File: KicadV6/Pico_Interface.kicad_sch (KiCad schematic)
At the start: 3 parts, among them J1 Conn_02x05_Odd_Even, J2 Conn_01x03_Male, U1 Pico

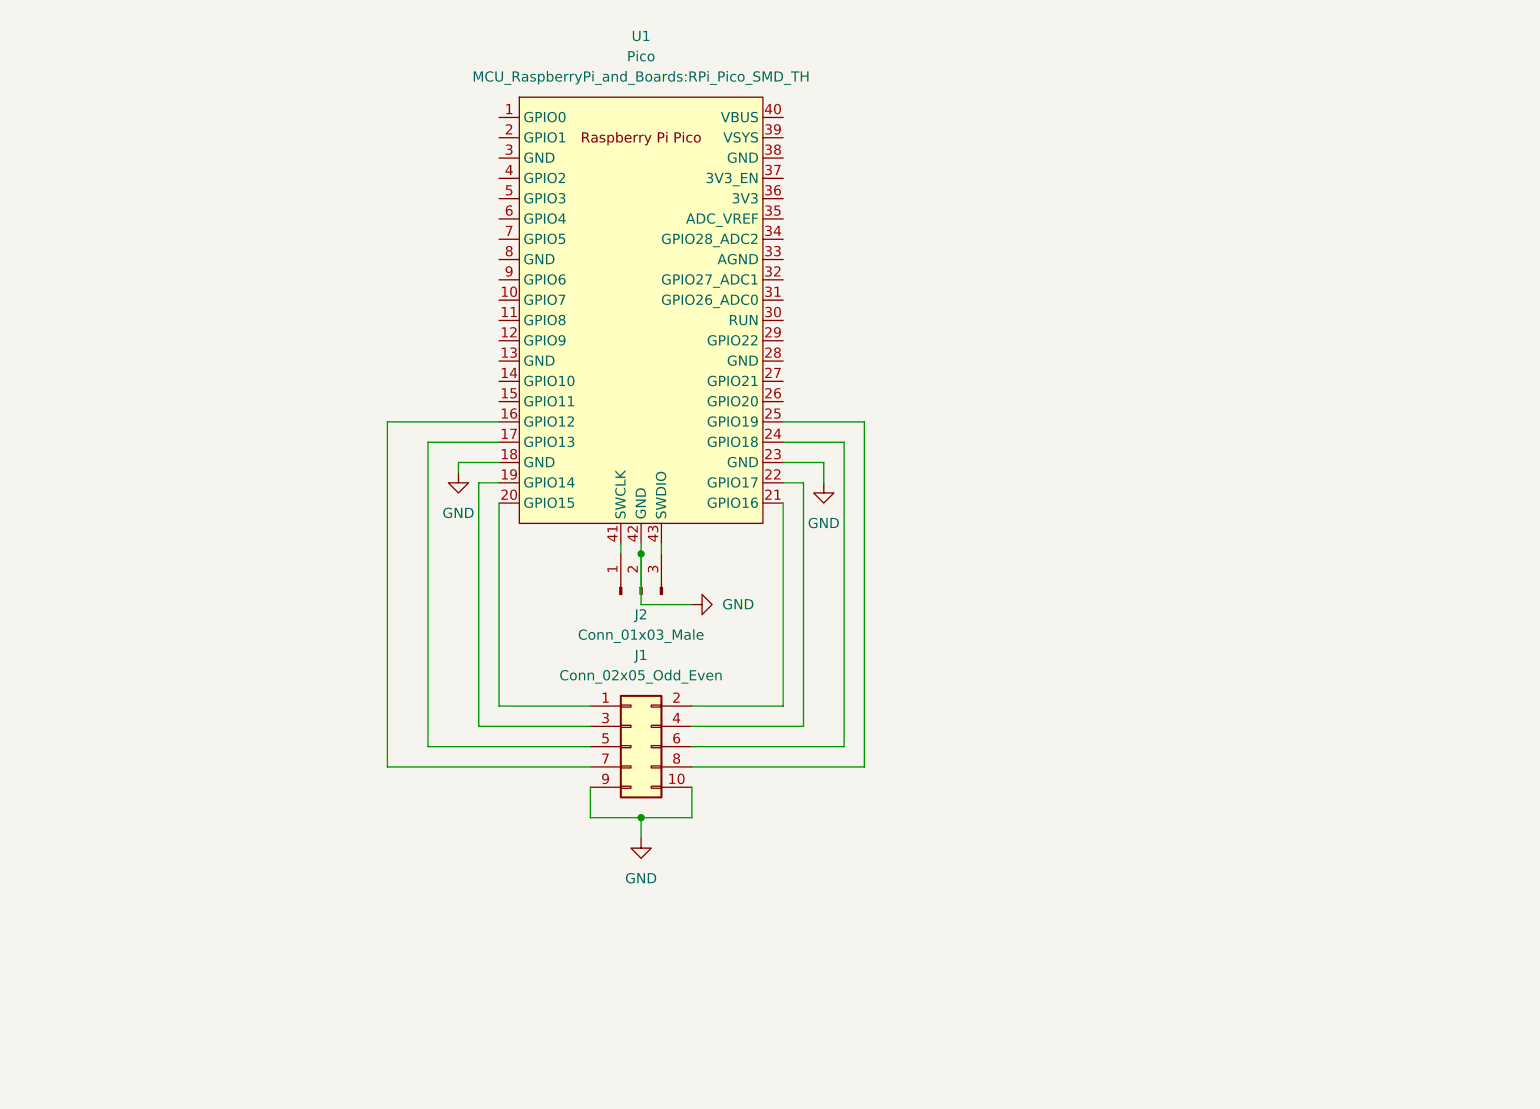
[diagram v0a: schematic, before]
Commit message: Added 4 PMOD / IDC Connectors
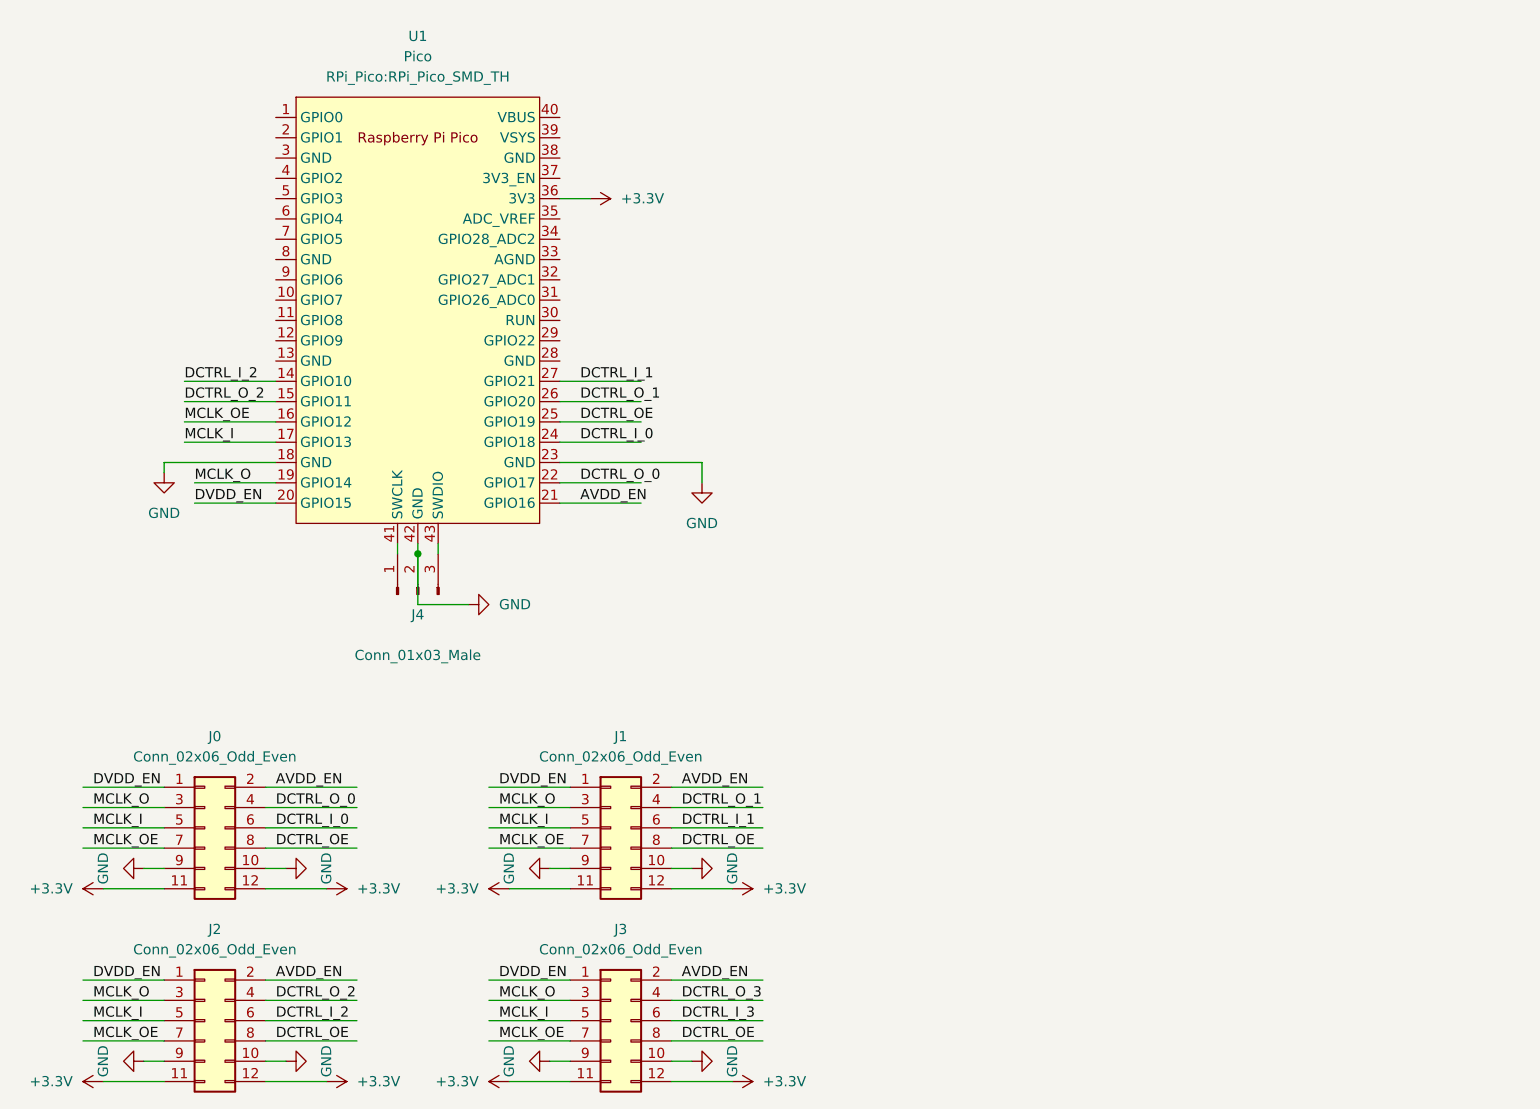
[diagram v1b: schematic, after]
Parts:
- removed J1: Conn_02x05_Odd_Even, Connector_IDC:IDC-Header_2x05_P2.54mm_Horizontal, symbol Connector_Generic:Conn_02x05_Odd_Even
- added J0, J1, J2, J3: Conn_02x06_Odd_Even, Connector_IDC:IDC-Header_2x06_P2.54mm_Vertical, symbol Connector_Generic:Conn_02x06_Odd_Even
- U1: footprint MCU_RaspberryPi_and_Boards:RPi_Pico_SMD_TH -> RPi_Pico:RPi_Pico_SMD_TH
- renumbered J2 to J4
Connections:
- net GND: now also J0.10 (Pin_10), J0.9 (Pin_9), J1.10 (Pin_10), J1.9 (Pin_9), J2.10 (Pin_10), J2.9 (Pin_9), J3.10 (Pin_10), J3.9 (Pin_9)
- net DVDD_EN: now reaches U1.20 (GPIO15)
- net DVDD_EN: now also J0.1 (Pin_1), J1.1 (Pin_1), J2.1 (Pin_1), J3.1 (Pin_1)
- net AVDD_EN: now reaches U1.21 (GPIO16)
- net AVDD_EN: now also J0.2 (Pin_2), J1.2 (Pin_2), J2.2 (Pin_2), J3.2 (Pin_2)
- net MCLK_O: now reaches U1.19 (GPIO14)
- net MCLK_O: now also J0.3 (Pin_3), J1.3 (Pin_3), J2.3 (Pin_3), J3.3 (Pin_3)
- net DCTRL_O_0: now reaches U1.22 (GPIO17)
- net DCTRL_O_0: now also J0.4 (Pin_4)
- net MCLK_I: now reaches U1.17 (GPIO13)
- net MCLK_I: now also J0.5 (Pin_5), J1.5 (Pin_5), J2.5 (Pin_5), J3.5 (Pin_5)
- net DCTRL_I_0: now reaches U1.24 (GPIO18)
- net DCTRL_I_0: now also J0.6 (Pin_6)
- net MCLK_OE: now reaches U1.16 (GPIO12)
- net MCLK_OE: now also J0.7 (Pin_7), J1.7 (Pin_7), J2.7 (Pin_7), J3.7 (Pin_7)
- net DCTRL_OE: now reaches U1.25 (GPIO19)
- net DCTRL_OE: now also J0.8 (Pin_8), J1.8 (Pin_8), J2.8 (Pin_8), J3.8 (Pin_8)
- net DCTRL_I_2: now reaches U1.14 (GPIO10)
- net DCTRL_I_2: now also J2.6 (Pin_6)
- net DCTRL_O_2: now reaches U1.15 (GPIO11)
- net DCTRL_O_2: now also J2.4 (Pin_4)
- net DCTRL_O_1: now reaches U1.26 (GPIO20)
- net DCTRL_O_1: now also J1.4 (Pin_4)
- net DCTRL_I_1: now reaches U1.27 (GPIO21)
- net DCTRL_I_1: now also J1.6 (Pin_6)
- net +3.3V: now reaches U1.36 (3V3)
- net +3.3V: now also J0.11 (Pin_11), J0.12 (Pin_12), J1.11 (Pin_11), J1.12 (Pin_12), J2.11 (Pin_11), J2.12 (Pin_12), J3.11 (Pin_11), J3.12 (Pin_12)
- new net DCTRL_I_3: J3.6 (Pin_6)
- new net DCTRL_O_3: J3.4 (Pin_4)
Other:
- moved on the sheet: J4

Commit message: Started change of layout
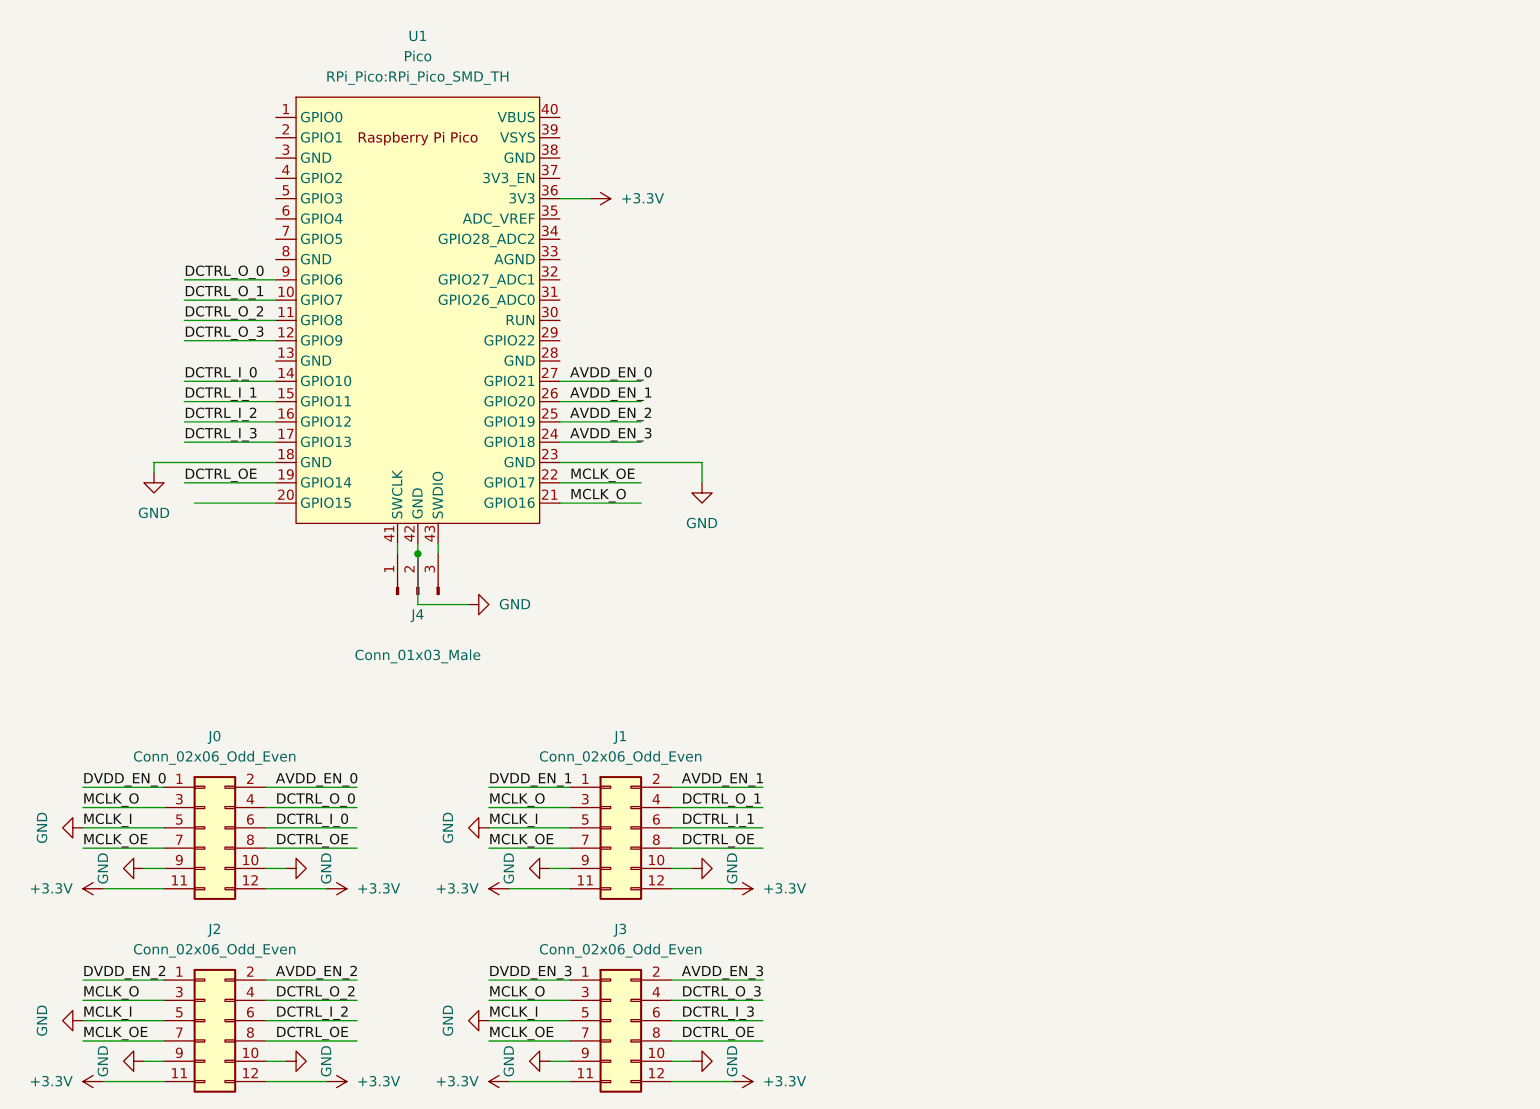
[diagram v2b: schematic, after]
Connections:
- net DCTRL_I_0: now also U1.14 (GPIO10); no longer U1.24 (GPIO18)
- net DCTRL_I_1: now also U1.15 (GPIO11); no longer U1.27 (GPIO21)
- net DCTRL_I_2: now also U1.16 (GPIO12); no longer U1.14 (GPIO10)
- net DCTRL_I_3: now also U1.17 (GPIO13)
- net DCTRL_OE: now also U1.19 (GPIO14); no longer U1.25 (GPIO19)
- net DCTRL_O_0: now also U1.9 (GPIO6); no longer U1.22 (GPIO17)
- net DCTRL_O_1: now also U1.10 (GPIO7); no longer U1.26 (GPIO20)
- net DCTRL_O_2: now also U1.11 (GPIO8); no longer U1.15 (GPIO11)
- net DCTRL_O_3: now also U1.12 (GPIO9)
- net GND: now also J0.5 (Pin_5), J1.5 (Pin_5), J2.5 (Pin_5), J3.5 (Pin_5)
- net MCLK_O: now also U1.21 (GPIO16); no longer U1.19 (GPIO14)
- net MCLK_OE: now also U1.22 (GPIO17); no longer U1.16 (GPIO12)
- removed net AVDD_EN: J0.2 (Pin_2), J1.2 (Pin_2), J2.2 (Pin_2), J3.2 (Pin_2), U1.21 (GPIO16)
- removed net DVDD_EN: J0.1 (Pin_1), J1.1 (Pin_1), J2.1 (Pin_1), J3.1 (Pin_1), U1.20 (GPIO15)
- removed net MCLK_I: J0.5 (Pin_5), J1.5 (Pin_5), J2.5 (Pin_5), J3.5 (Pin_5), U1.17 (GPIO13)
- new net AVDD_EN_0: J0.2 (Pin_2), U1.27 (GPIO21)
- new net AVDD_EN_1: J1.2 (Pin_2), U1.26 (GPIO20)
- new net AVDD_EN_2: J2.2 (Pin_2), U1.25 (GPIO19)
- new net AVDD_EN_3: J3.2 (Pin_2), U1.24 (GPIO18)
- new net DVDD_EN_0: J0.1 (Pin_1)
- new net DVDD_EN_1: J1.1 (Pin_1)
- new net DVDD_EN_2: J2.1 (Pin_1)
- new net DVDD_EN_3: J3.1 (Pin_1)

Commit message: Added Trigger/Bussy and 3.3V LDO
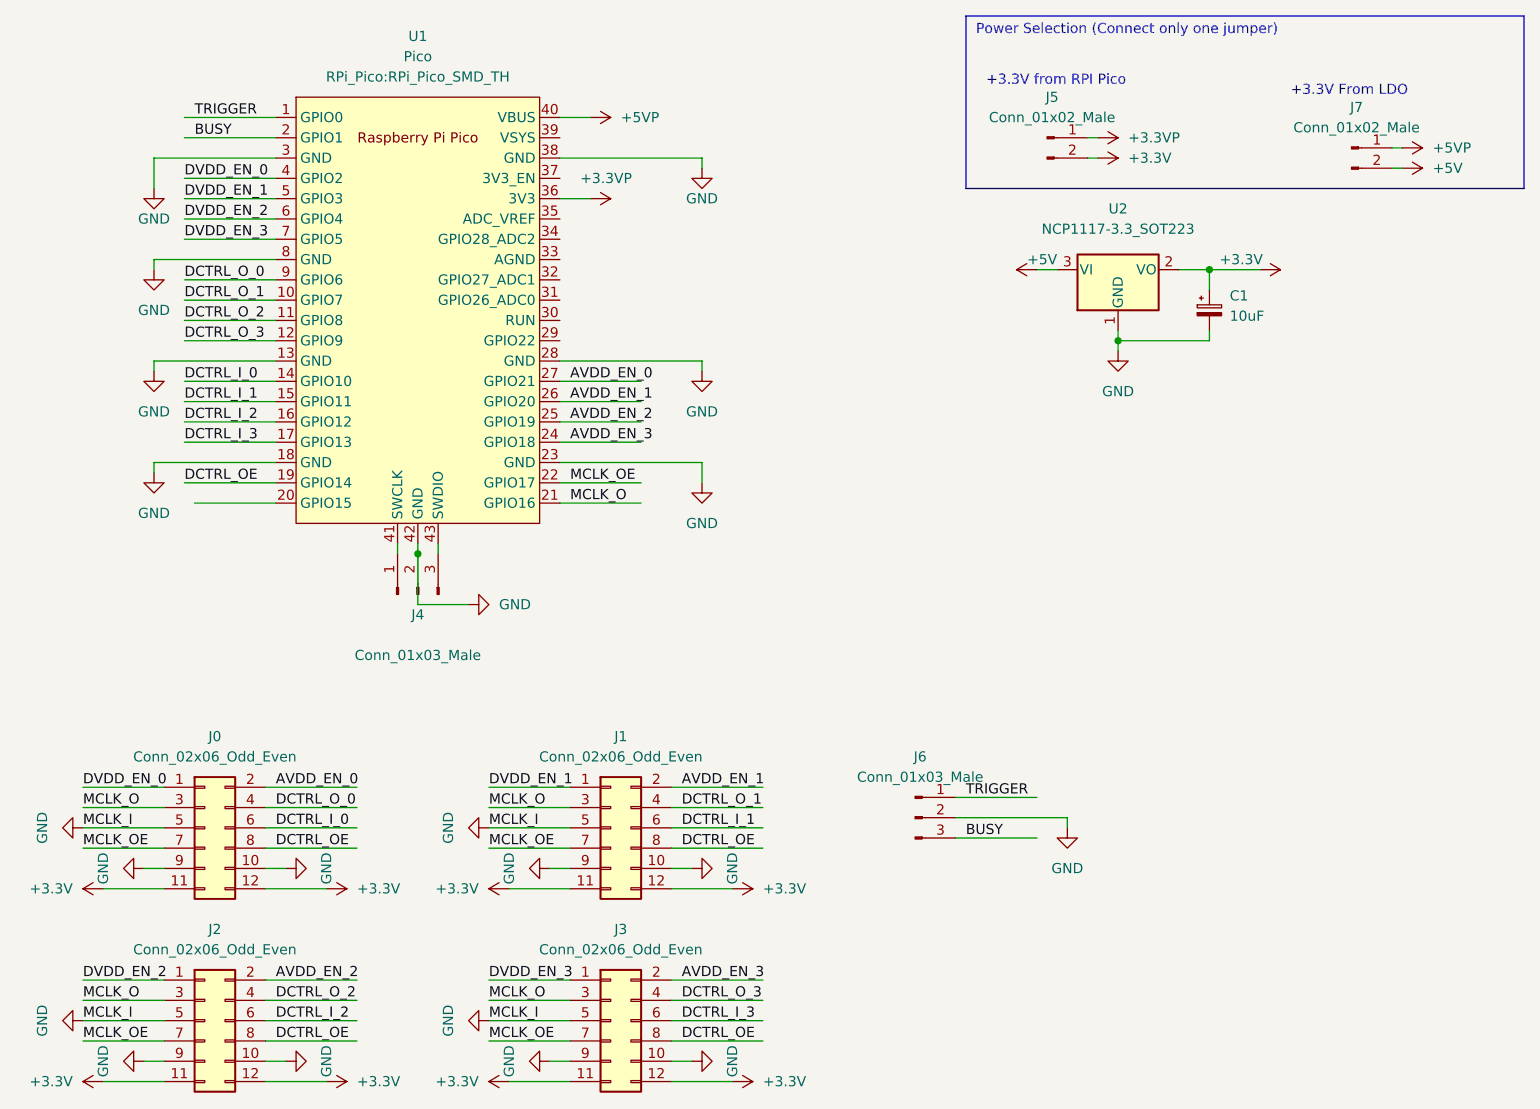
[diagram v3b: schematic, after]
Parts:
- added C1: 10uF, Capacitor_SMD:C_1206_3216Metric_Pad1.33x1.80mm_HandSolder, symbol Device:C_Polarized_Small
- added J5, J7: Conn_01x02_Male, Connector_PinHeader_2.54mm:PinHeader_1x02_P2.54mm_Vertical, symbol Connector:Conn_01x02_Male
- added J6: Conn_01x03_Male, Connector_PinHeader_2.54mm:PinHeader_1x03_P2.54mm_Vertical, symbol Connector:Conn_01x03_Male
- added U2: NCP1117-3.3_SOT223, Package_TO_SOT_SMD:SOT-223-3_TabPin2, symbol Regulator_Linear:NCP1117-3.3_SOT223
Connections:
- net +3.3V: now also C1.1, J5.2 (Pin_2), U2.2 (VO); no longer U1.36 (3V3)
- net DVDD_EN_0: now also U1.4 (GPIO2)
- net DVDD_EN_1: now also U1.5 (GPIO3)
- net DVDD_EN_2: now also U1.6 (GPIO4)
- net DVDD_EN_3: now also U1.7 (GPIO5)
- net GND: now also U1.13 (GND), U1.28 (GND), U1.3 (GND), U1.38 (GND), U1.8 (GND), C1.2, J6.2 (Pin_2), U2.1 (GND)
- net TRIGGER: now reaches U1.1 (GPIO0)
- net TRIGGER: now also J6.1 (Pin_1)
- net BUSY: now reaches U1.2 (GPIO1)
- net BUSY: now also J6.3 (Pin_3)
- net +5VP: now reaches U1.40 (VBUS)
- net +5VP: now also J7.1 (Pin_1)
- new net +3.3VP: J5.1 (Pin_1), U1.36 (3V3)
- new net +5V: J7.2 (Pin_2), U2.3 (VI)
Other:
- note added: "+3.3V From LDO"
- note added: "+3.3V from RPI Pico"
- note added: "Power Selection (Connect only one jumper)"

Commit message: Added new Col to BOM (Farnell Order URL)
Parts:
- C1: Farnell URL (none) -> https://no.farnell.com/tdk/cga5l1x7r1e106k160ac/cap-10-f-25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
- J0, J1, J2, J3: Farnell URL (none) -> https://no.farnell.com/multicomp/mc-254-12-00-st-dip/connec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
- U1: Farnell URL (none) -> https://no.farnell.com/raspberry-pi/raspberry-pi-pico/raspb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
- U2: Farnell URL (none) -> https://no.farnell.com/on-semiconductor/ncp1117st33t3g/ic-l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
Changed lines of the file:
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@@
     (property "Value" "Pico" (id 1) (at 74.93 53.34 0))
     (property "Footprint" "RPi_Pico:RPi_Pico_SMD_TH" (id 2) (at 74.93 55.88 0))
-    (property "Datasheet" "" (id 3) (at 74.93 85.09 0)
+    (property "Datasheet" "https://www.farnell.com/datasheets/3189214.pdf" (id 3) (at 74.93 85.09 0)
+      (effects (font (size 1.27 1.27)) hide)
+    )
+    (property "Farnell URL" "https://no.farnell.com/raspberry-pi/raspberry-pi-pico/raspberry-pi-32bit-arm-cortex/dp/3643332?st=rp2040%20%20pico" (id 4) (at 74.93 85.09 0)
       (effects (font (size 1.27 1.27)) hide)
     )
@@
       (effects (font (size 1.27 1.27)) hide)
     )
+    (property "Farnell URL" "https://no.farnell.com/multicomp/mc-254-12-00-st-dip/connector-header-12pos-2row-2/dp/2843528?st=din%2041651%2012%20header" (id 4) (at 99.06 149.86 0)
+      (effects (font (size 1.27 1.27)) hide)
+    )
     (pin "1")
     (pin "10")
@@
       (effects (font (size 1.27 1.27)) hide)
     )
+    (property "Farnell URL" "https://no.farnell.com/multicomp/mc-254-12-00-st-dip/connector-header-12pos-2row-2/dp/2843528?st=din%2041651%2012%20header" (id 4) (at 48.26 149.86 0)
+      (effects (font (size 1.27 1.27)) hide)
+    )
     (pin "1")
     (pin "10")
@@
       (effects (font (size 1.27 1.27)) hide)
     )
+    (property "Farnell URL" "https://no.farnell.com/multicomp/mc-254-12-00-st-dip/connector-header-12pos-2row-2/dp/2843528?st=din%2041651%2012%20header" (id 4) (at 99.06 173.99 0)
+      (effects (font (size 1.27 1.27)) hide)
+    )
     (pin "1")
     (pin "10")
@@
       (effects (font (size 1.27 1.27)) hide)
     )
+    (property "Farnell URL" "https://no.farnell.com/on-semiconductor/ncp1117st33t3g/ic-linear-voltage-regulator/dp/1652366" (id 4) (at 162.56 80.01 0)
+      (effects (font (size 1.27 1.27)) hide)
+    )
     (pin "1")
     (pin "2")
@@
       (effects (font (size 1.27 1.27)) hide)
     )
-    (property "Datasheet" "~" (id 3) (at 173.99 85.09 0)
+    (property "Datasheet" "https://4donline.ihs.com/images/VipMasterIC/IC/TDKC/TDKC-S-A0013942978/TDKC-S-A0013942978-1.pdf?hkey=6D3A4C79FDBF58556ACFDE234799DDF0" (id 3) (at 173.99 85.09 0)
+      (effects (font (size 1.27 1.27)) hide)
+    )
+    (property "Farnell URL" "https://no.farnell.com/tdk/cga5l1x7r1e106k160ac/cap-10-f-25v-10-x7r-1206/dp/2211068" (id 4) (at 173.99 85.09 0)
       (effects (font (size 1.27 1.27)) hide)
     )
@@
       (effects (font (size 1.27 1.27)) hide)
     )
+    (property "Farnell URL" "https://no.farnell.com/multicomp/mc-254-12-00-st-dip/connector-header-12pos-2row-2/dp/2843528?st=din%2041651%2012%20header" (id 4) (at 48.26 173.99 0)
+      (effects (font (size 1.27 1.27)) hide)
+    )

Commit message: BOM Update
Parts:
- C1: Farnell URL https://no.farnell.com/tdk/cga5l1x7r1e106k160ac/cap-10-f-25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 -> https://no.farnell.com/kemet/t491a106k016at/cap-10-f-16v-10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
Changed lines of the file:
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@@
       (effects (font (size 1.27 1.27)) hide)
     )
-    (property "Datasheet" "https://4donline.ihs.com/images/VipMasterIC/IC/TDKC/TDKC-S-A0013942978/TDKC-S-A0013942978-1.pdf?hkey=6D3A4C79FDBF58556ACFDE234799DDF0" (id 3) (at 173.99 85.09 0)
+    (property "Datasheet" "https://4donline.ihs.com/images/VipMasterIC/IC/KEME/KEME-S-A0006487387/KEME-S-A0006487387-1.pdf?hkey=52A5661711E402568146F3353EA87419" (id 3) (at 173.99 85.09 0)
       (effects (font (size 1.27 1.27)) hide)
     )
-    (property "Farnell URL" "https://no.farnell.com/tdk/cga5l1x7r1e106k160ac/cap-10-f-25v-10-x7r-1206/dp/2211068" (id 4) (at 173.99 85.09 0)
+    (property "Farnell URL" "https://no.farnell.com/kemet/t491a106k016at/cap-10-f-16v-10-1206-smd/dp/1457414" (id 4) (at 173.99 85.09 0)
       (effects (font (size 1.27 1.27)) hide)
     )
